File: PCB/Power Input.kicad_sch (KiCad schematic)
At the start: 2 parts

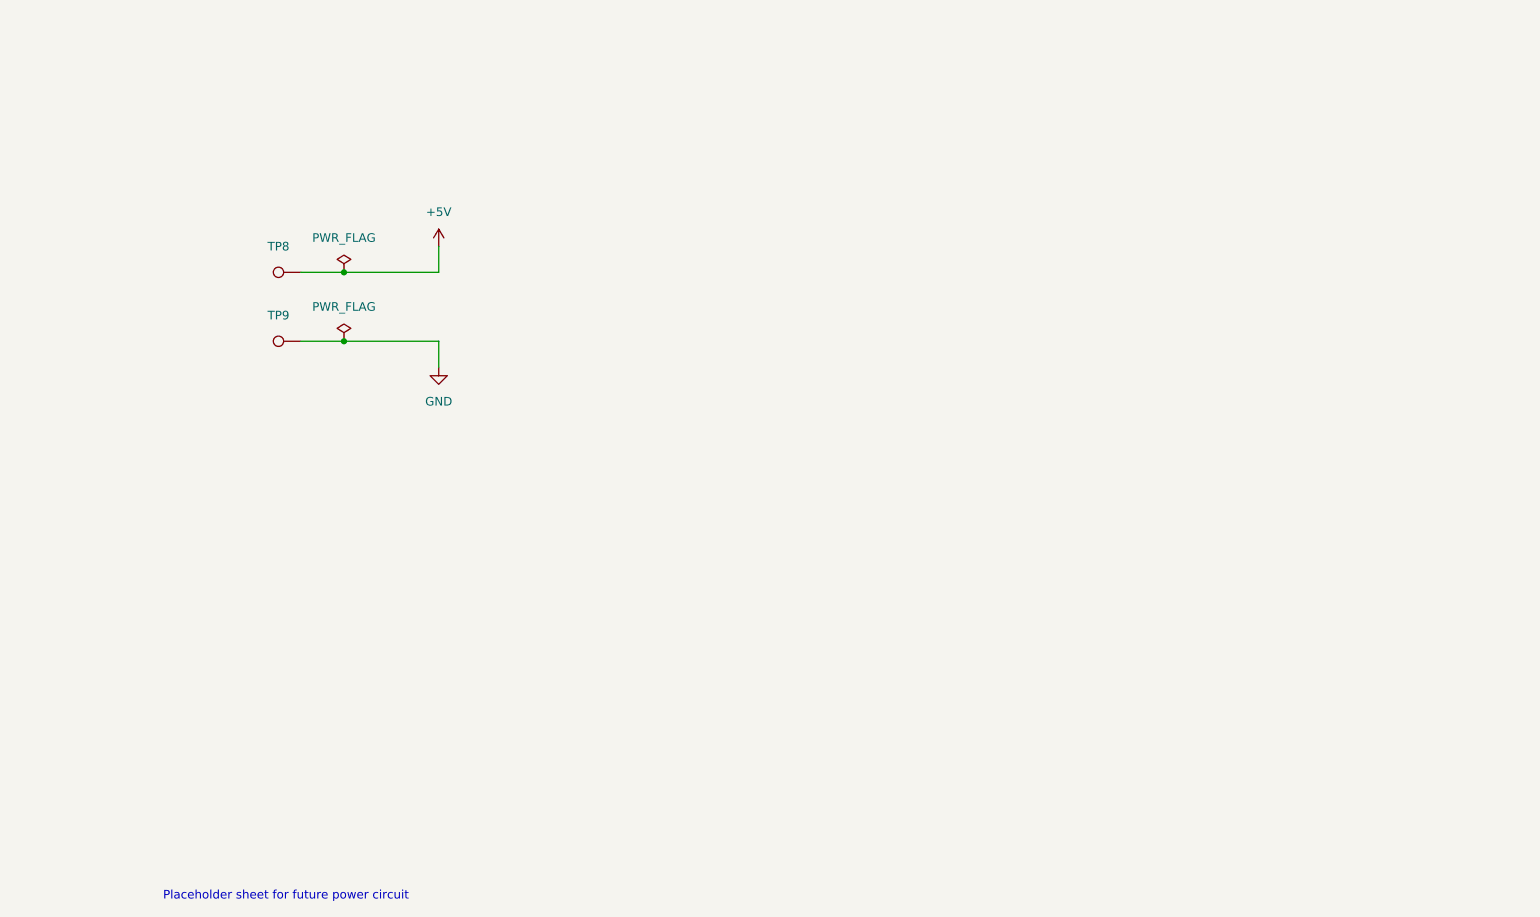
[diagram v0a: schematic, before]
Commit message: Added FUSB302B and associated circuitry.
Added FUSB302B, along with USB-C Connector and LDO.  The LDO is
needed to power the FUSB302B from the cable.

Also added some debugging and convenience items such as a QWIIC
connector and some test points.
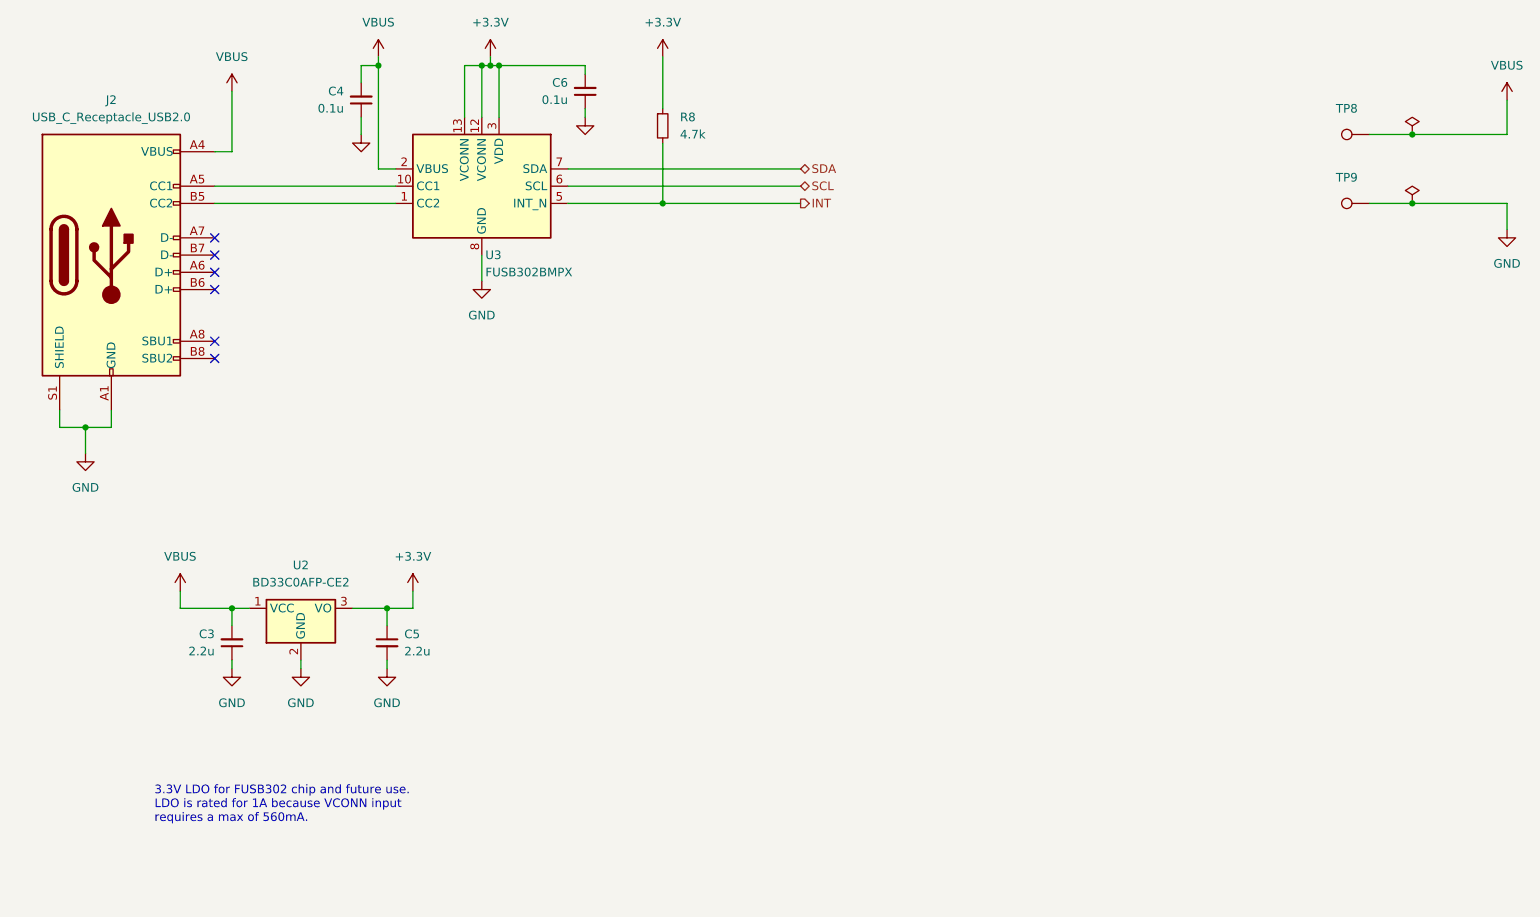
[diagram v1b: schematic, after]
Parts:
- added C3, C5: 2.2u, Capacitor_SMD:C_0805_2012Metric, symbol Device:C_Small
- added C4, C6: 0.1u, Capacitor_SMD:C_0402_1005Metric_Pad0.74x0.62mm_HandSolder, symbol Device:C_Small
- added J2: USB_C_Receptacle_USB2.0, Connector_USB:USB_C_Receptacle_GCT_USB4085, symbol Connector:USB_C_Receptacle_USB2.0
- added R8: 4.7k, Resistor_SMD:R_0402_1005Metric_Pad0.72x0.64mm_HandSolder, symbol Device:R_Small
- added U2: BD33C0AFP-CE2, Package_TO_SOT_SMD:TO-252-2, symbol battery simulator:BD33C0AFP-CE2
- added U3: FUSB302BMPX, Package_DFN_QFN:WQFN-14-1EP_2.5x2.5mm_P0.5mm_EP1.45x1.45mm, symbol Interface_USB:FUSB302BMPX
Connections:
- net GND: now also C3.1, C4.1, C5.2, C6.1, J2.A1 (GND), J2.A12 (GND), J2.B1 (GND), J2.B12 (GND), J2.S1 (SHIELD), U2.2 (GND), U3.15 (GND), U3.8 (GND), U3.9 (GND)
- net +5V renamed VBUS
- net VBUS: now also C3.2, C4.2, J2.A4 (VBUS), J2.A9 (VBUS), J2.B4 (VBUS), J2.B9 (VBUS), U2.1 (VCC), U3.2 (VBUS)
- new net: J2.A5 (CC1), U3.10 (CC1), U3.11 (CC1)
- new net: J2.B5 (CC2), U3.1 (CC2), U3.14 (CC2)
- new net +3.3V: C5.1, C6.2, R8.1, U2.3 (VO), U3.12 (VCONN), U3.13 (VCONN), U3.3 (VDD), U3.4 (VDD)
- new net INT: R8.2, U3.5 (INT_N)
- new net SCL: U3.6 (SCL)
- new net SDA: U3.7 (SDA)
- no-connect marks 0 -> 6
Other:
- note added: "3.3V LDO for FUSB302 chip and future use. LDO is rated for 1A because VCONN input requires a max of 560mA."
- note removed: "Placeholder sheet for future power circuit"
- moved on the sheet: TP8, TP9

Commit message: Imported and placed all components into PCB.
Imported all components into PCB.  Finalized PCB outline to 50mm x
50mm square.  Arranged all components into reasonable locations
and added 2 planes.

Schematic update is just adding netlabels to the CC1 and CC2 nets.
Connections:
- net CC1: now reaches J2.A5 (CC1), U3.10 (CC1), U3.11 (CC1)
- net CC2: now reaches J2.B5 (CC2), U3.1 (CC2), U3.14 (CC2)
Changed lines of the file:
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@@
+    (effects (font (size 1.27 1.27)) (justify left bottom))
+  )
+  (label "CC1" (at 71.12 62.23 0)
+    (effects (font (size 1.27 1.27)) (justify left bottom))
+  )
+  (label "CC2" (at 71.12 64.77 0)
     (effects (font (size 1.27 1.27)) (justify left bottom))
   )

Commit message: Update to KiCAD v7, and finalize for V1 build
Updated to KiCAD v7, which touched many files.

Also made some changes to finalize board for prototype build.  Simplified the
circuit a bit to just something built and tested.
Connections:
- net at J2.A6 (D+): now also J2.B6 (D+)
- net at J2.A7 (D-): now also J2.B7 (D-)
- no-connect marks 6 -> 2
